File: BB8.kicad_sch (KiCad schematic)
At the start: 2 parts

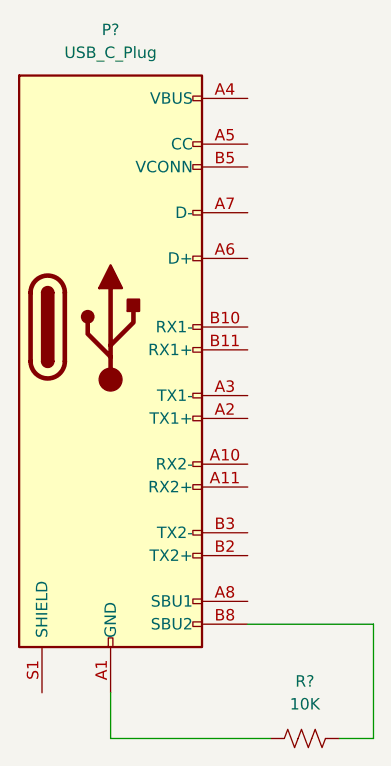
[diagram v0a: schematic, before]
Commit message: Update circuit and add PCB design
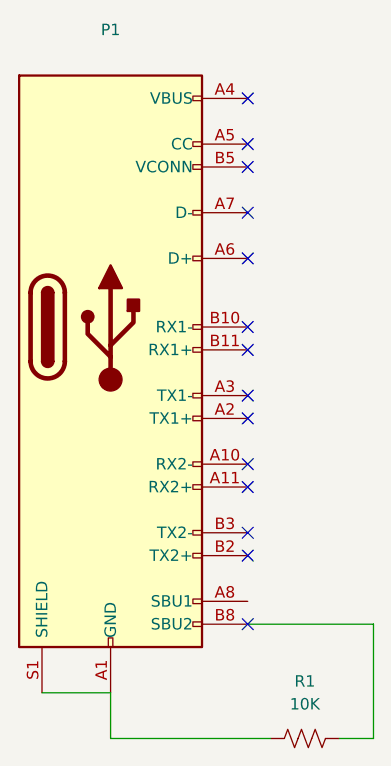
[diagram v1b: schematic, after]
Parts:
- P1: renamed from P?; value USB_C_Plug -> (none)
- R1: renamed from R?; footprint (none) -> Resistor_THT:R_Axial_DIN0207_L6.3mm_D2.5mm_P10.16mm_Horizontal
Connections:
- net at P1.A1 (GND), P1.A12 (GND), P1.B1 (GND)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: now also P1.S1 (SHIELD)
- no-connect marks 0 -> 14
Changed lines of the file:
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@@
 (kicad_sch (version 20211123) (generator eeschema)
   (paper "A4")
+  (no_connect (at 110.49 121.92))
+  (no_connect (at 110.49 114.3))
+  (no_connect (at 110.49 104.14))
+  (no_connect (at 110.49 106.68))
+  (no_connect (at 110.49 111.76))
+  (no_connect (at 110.49 63.5))
+  (no_connect (at 110.49 68.58))
+  (no_connect (at 110.49 71.12))
+  (no_connect (at 110.49 76.2))
+  (no_connect (at 110.49 81.28))
+  (no_connect (at 110.49 88.9))
+  (no_connect (at 110.49 91.44))
+  (no_connect (at 110.49 96.52))
+  (no_connect (at 110.49 99.06))
   (wire (pts (xy 124.46 121.92) (xy 124.46 134.62))
     (stroke (width 0) (type default) (color 0 0 0 0))
@@
     (stroke (width 0) (type default) (color 0 0 0 0))
   )
-  (wire (pts (xy 124.46 121.92) (xy 110.49 121.92))
+  (wire (pts (xy 87.63 129.54) (xy 95.25 129.54))
+    (stroke (width 0) (type default) (color 0 0 0 0))
+  )
+  (wire (pts (xy 110.49 121.92) (xy 124.46 121.92))
     (stroke (width 0) (type default) (color 0 0 0 0))
   )
@@
   (symbol (lib_id "Connector:USB_C_Plug") (at 95.25 88.9 0) (unit 1)
     (in_bom yes) (on_board yes) (fields_autoplaced)
-    (property "Reference" "P?" (id 0) (at 95.25 55.88 0))
-    (property "Value" "USB_C_Plug" (id 1) (at 95.25 58.42 0))
+    (property "Reference" "P1" (id 0) (at 95.25 55.88 0))
+    (property "Value" "" (id 1) (at 95.25 58.42 0))
     (property "Footprint" "" (id 2) (at 99.06 88.9 0)
       (effects (font (size 1.27 1.27)) hide)
@@
   (symbol (lib_id "Device:R_US") (at 116.84 134.62 270) (unit 1)
     (in_bom yes) (on_board yes) (fields_autoplaced)
-    (property "Reference" "R?" (id 0) (at 116.84 128.27 90))
+    (property "Reference" "R1" (id 0) (at 116.84 128.27 90))
     (property "Value" "10K" (id 1) (at 116.84 130.81 90))
-    (property "Footprint" "" (id 2) (at 116.586 135.636 90)
+    (property "Footprint" "Resistor_THT:R_Axial_DIN0207_L6.3mm_D2.5mm_P10.16mm_Horizontal" (id 2) (at 116.586 135.636 90)
       (effects (font (size 1.27 1.27)) hide)
     )
@@
   (symbol_instances
     (path "/501e1496-be22-4cee-8b4c-cbf8c46e7943"
-      (reference "P?") (unit 1) (value "USB_C_Plug") (footprint "")
+      (reference "P1") (unit 1) (value "USB_C_Plug") (footprint "Connector_USB:USB_C_Plug_JAE_DX07P024AJ1")
     )
     (path "/bfa9bd3e-6c00-40c9-ac42-43d7623e6f77"
-      (reference "R?") (unit 1) (value "10K") (footprint "")
+      (reference "R1") (unit 1) (value "10K") (footprint "Resistor_THT:R_Axial_DIN0207_L6.3mm_D2.5mm_P10.16mm_Horizontal")
     )
   )
